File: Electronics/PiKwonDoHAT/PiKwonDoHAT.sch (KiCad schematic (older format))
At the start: 45 parts, among them J1 Conn_02x20_Odd_Even, J2 Judge3, J3 Judge2, J4 Judge1, J5 Controller, U1 74LV1T34, U2 74LV1T34, U3 74LV1T34, U4 74LV1T34

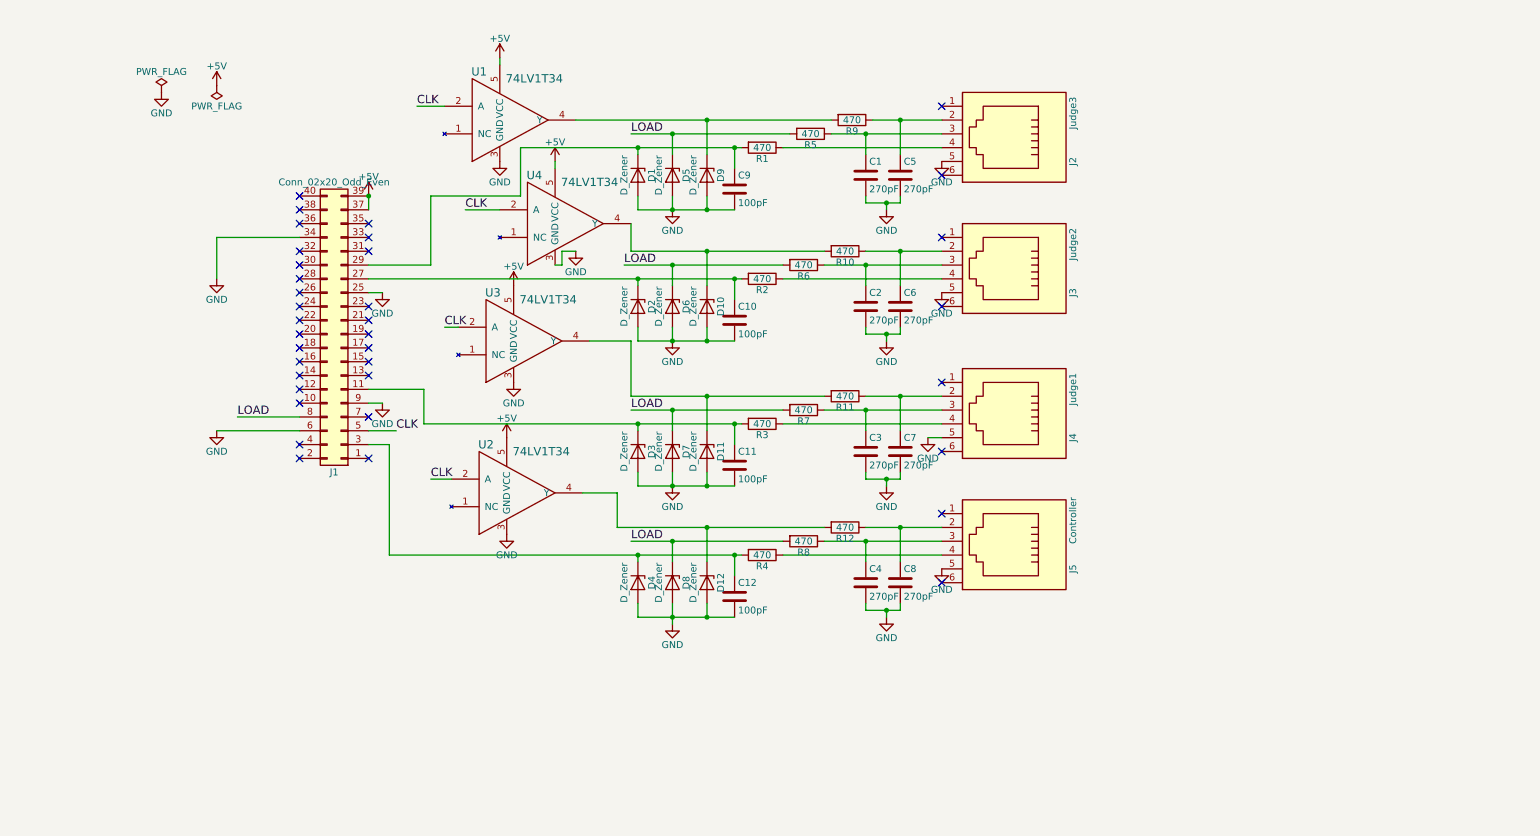
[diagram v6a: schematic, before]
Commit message: Completed HAT PCB
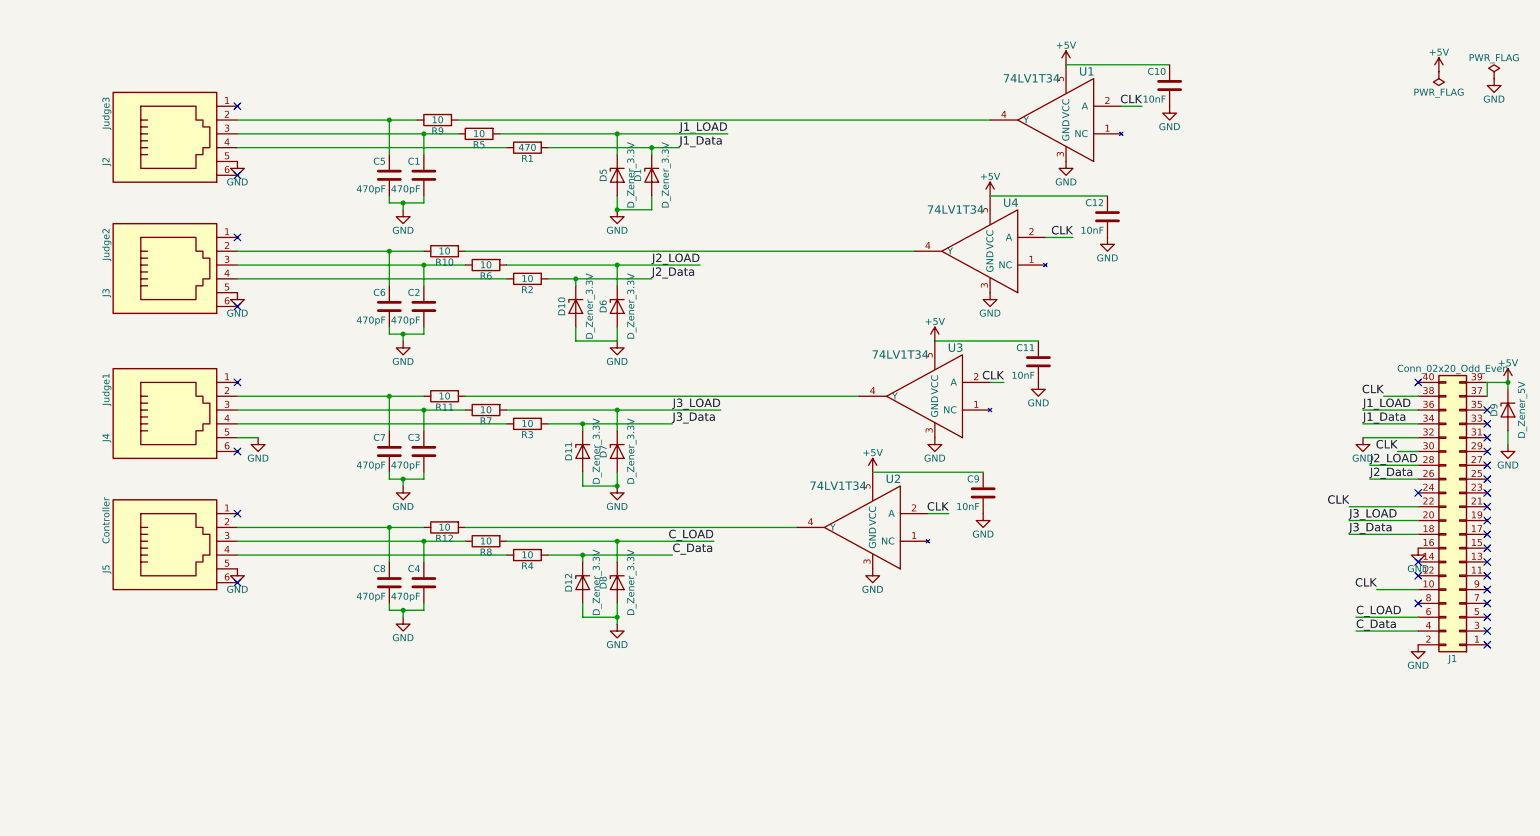
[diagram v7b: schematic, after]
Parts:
- removed D2, D3, D4: D_Zener, Diodes_SMD:SOD-80C, symbol D_Zener
- C1, C2, C3, C4, C5, C6, C7, C8: value 270pF -> 470pF
- C10, C11, C12, C9: value 100pF -> 10nF
- D1, D10, D11, D12, D5, D6, D7, D8: value D_Zener -> D_Zener_3.3V
- D9: value D_Zener -> D_Zener_5V
- R10, R11, R12, R2, R3, R4, R5, R6, R7, R8, R9: value 470 -> 10
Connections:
- net +5V: now also C10.1, C11.1, C12.1, C9.1, D9.1 (K)
- net CLK: now also J1.10 (Pin_10), J1.22 (Pin_22), J1.30 (Pin_30), J1.38 (Pin_38); no longer J1.5 (Pin_5)
- net GND: now also J1.16 (Pin_16), J1.2 (Pin_2), J1.32 (Pin_32); no longer J1.25 (Pin_25), J1.34 (Pin_34), J1.6 (Pin_6), J1.9 (Pin_9)
- net J3_Data: now reaches J1.18 (Pin_18)
- net J3_Data: now also D11.1 (K), R3.2
- net J3_LOAD: now reaches J1.20 (Pin_20)
- net J3_LOAD: now also D7.1 (K), R7.2
- net J2_Data: now reaches J1.26 (Pin_26)
- net J2_Data: now also D10.1 (K), R2.2
- net J2_LOAD: now reaches J1.28 (Pin_28)
- net J2_LOAD: now also D6.1 (K), R6.2
- net J1_Data: now reaches D1.1 (K), R1.2
- net J1_Data: now also J1.34 (Pin_34); no longer C9.1, J1.29 (Pin_29)
- net J1_LOAD: now reaches J1.36 (Pin_36)
- net J1_LOAD: now also D5.1 (K), R5.2
- net C_Data: now reaches J1.4 (Pin_4)
- net C_Data: now also D12.1 (K), R4.2
- net at R9.2, U1.4 (Y): no longer D9.1 (K)
- net at R10.2, U4.4 (Y): no longer D10.1 (K)
- net at R11.2, U3.4 (Y): no longer D11.1 (K)
- net at R12.2, U2.4 (Y): no longer D12.1 (K)
- removed net LOAD: D5.1 (K), D6.1 (K), D7.1 (K), D8.1 (K), J1.8 (Pin_8), R5.2, R6.2, R7.2, R8.2
- new net C_LOAD: D8.1 (K), J1.6 (Pin_6), R8.2
- now unconnected: J1.11 (Pin_11), J1.27 (Pin_27), J1.3 (Pin_3)
- no-connect marks 36 -> 31
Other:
- moved on the sheet: C1, C10, C2, C3, C4, C5, C6, C7, C8, D1, D10, D11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

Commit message: Tweaked and cleaned up hat schematic:
* Made all input resistors 470 ohms
* Cleaned up graphically
* Reassigned reference numbers
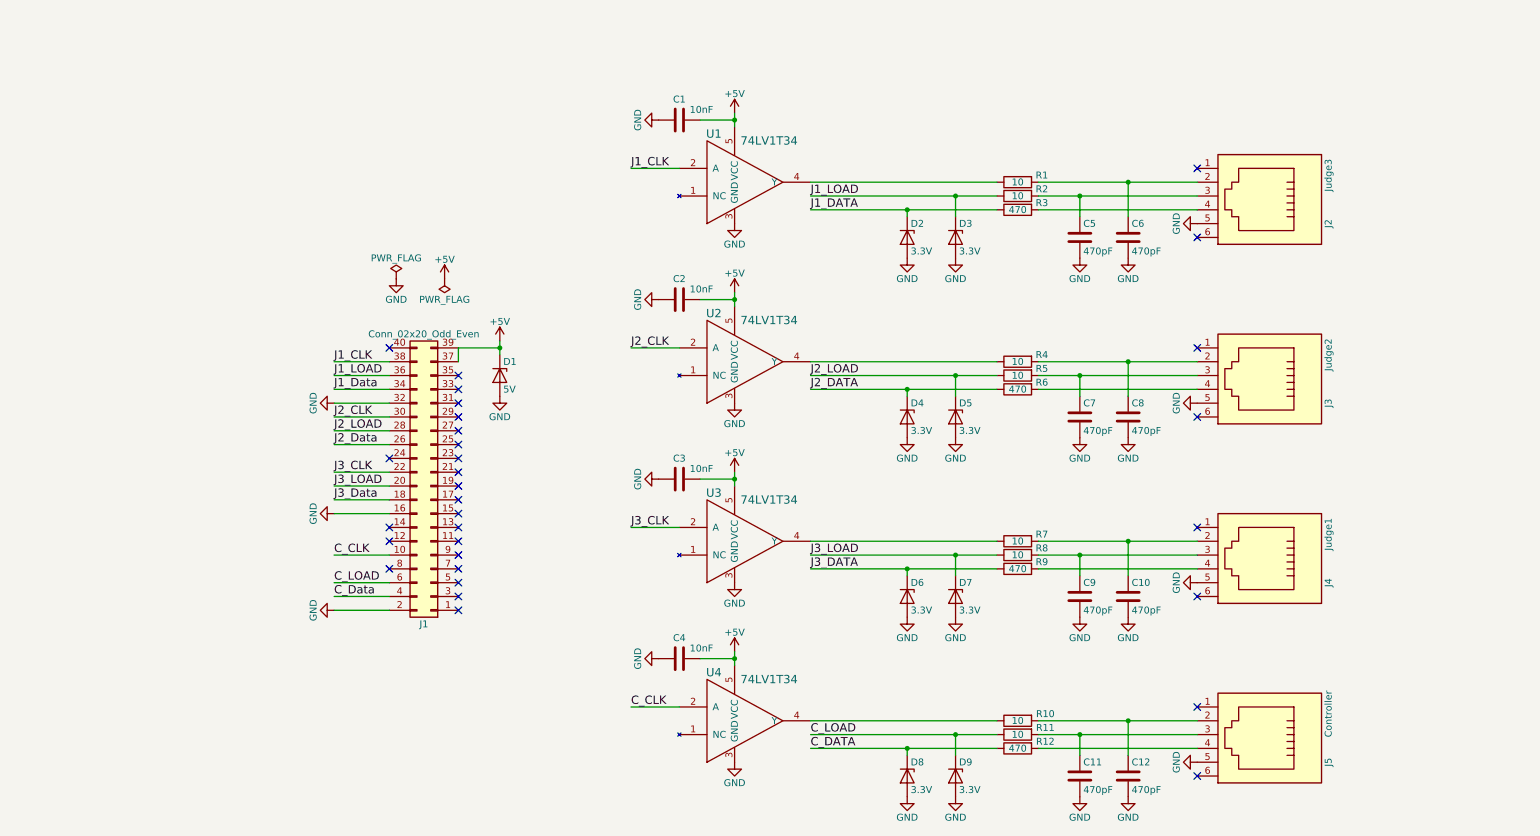
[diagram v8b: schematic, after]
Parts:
- removed C10, C11, C9: 10nF, Capacitors_SMD:C_0805_HandSoldering, symbol C
- removed D10, D11, D12: D_Zener_3.3V, Diodes_SMD:SOD-80C, symbol D_Zener
- removed R10: 10, Resistors_SMD:R_1206_HandSoldering, symbol R
- removed U2: 74LV1T34, TO_SOT_Packages_SMD:SOT-23-5_HandSoldering, symbol 74LV1T34
- added C1, C3, C4: 10nF, Capacitors_SMD:C_0805_HandSoldering, symbol C
- added D1: 5V, Diodes_SMD:SOD-80C, symbol D_Zener
- added D4, D5: 3.3V, Diodes_SMD:SOD-80C, symbol D_Zener
- added R12: 470, Resistors_SMD:R_1206_HandSoldering, symbol R
- added U4: 74LV1T34, TO_SOT_Packages_SMD:SOT-23-5_HandSoldering, symbol 74LV1T34
- D2: renamed from D1; value D_Zener_3.3V -> 3.3V
- D3: renamed from D5; value D_Zener_3.3V -> 3.3V
- D6, D7, D8: value D_Zener_3.3V -> 3.3V
- D9: value D_Zener_5V -> 3.3V
- R6: renamed from R2; value 10 -> 470
- R9: renamed from R3; value 10 -> 470
- renumbered C7 to C10, C4 to C11, C8 to C12, C12 to C2, C1 to C5, C5 to C6, C2 to C7, C6 to C8, C3 to C9, R9 to R1, R12 to R10, R5 to R2, R1 to R3, R6 to R5, U4 to U2
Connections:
- net +5V: now also C1.1, C3.1, C4.1, D1.1 (K), U4.5 (VCC); no longer D9.1 (K)
- net C_Data: no longer R4.2
- net C_LOAD: now also D9.1 (K), R11.1; no longer D8.1 (K), R8.2
- net GND: now also C1.2, C3.2, C4.2, D1.2 (A), D4.2 (A), D5.2 (A), U4.3 (GND)
- net J1_Data: no longer D2.1 (K), R3.2
- net J1_LOAD: now also R2.1; no longer R2.2
- net J2_Data: no longer R6.2
- net J2_LOAD: now also R5.1, D5.1 (K); no longer D6.1 (K), R5.2
- net J3_Data: no longer R9.2
- net J3_LOAD: now also R8.1; no longer R7.2
- net at C6.1, J2.2: now also R1.2; no longer R1.1
- net at C5.1, J2.3: now also R2.2; no longer R2.1
- net at J2.4: now also R3.2; no longer R3.1
- net at C8.1, J3.2: now also R4.2
- net at C7.1, J3.3: now also R5.2; no longer R5.1
- net at J3.4: now also R6.2; no longer R6.1
- net at C10.1, J4.2: now also R7.2; no longer R11.1
- net at C9.1, J4.3: now also R8.2; no longer R7.1
- net at J4.4: now also R9.2; no longer R9.1
- net at C12.1, J5.2: now also R10.2; no longer R10.1
- net at C11.1, J5.3: now also R11.2; no longer R8.1
- net at J5.4: now also R12.2; no longer R4.1
- net at U1.4 (Y): now also R1.1; no longer R1.2
- net at U2.4 (Y): now also R4.1
- net at U3.4 (Y): now also R7.1; no longer R11.2
- removed net CLK: J1.10 (Pin_10), J1.22 (Pin_22), J1.30 (Pin_30), J1.38 (Pin_38), U1.2 (A), U2.2 (A), U3.2 (A)
- new net: R10.1, U4.4 (Y)
- new net C_CLK: J1.10 (Pin_10), U4.2 (A)
- new net C_DATA: D8.1 (K), R12.1
- new net J1_CLK: J1.38 (Pin_38), U1.2 (A)
- new net J1_DATA: D2.1 (K), R3.1
- new net J2_CLK: J1.30 (Pin_30), U2.2 (A)
- new net J2_DATA: D4.1 (K), R6.1
- new net J3_CLK: J1.22 (Pin_22), U3.2 (A)
- new net J3_DATA: D6.1 (K), R9.1
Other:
- moved on the sheet: C10, C11, C12, C2, C5, C6, C7, C8, C9, D2, D3, J1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
